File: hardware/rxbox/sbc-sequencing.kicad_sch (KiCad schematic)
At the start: 0 parts

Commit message: supervisor + symbol, new journal. jumper for t113 power
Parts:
- added C19, C20: 68nF, symbol Device:C_Small
- added C21: 640nF, symbol Device:C_Small
- added D1, D2, D3: 1N4148, symbol Device:D_Small_Filled
- added R13, R14, R15, R16, R19, R21: 1MR, symbol Device:R_Small_US
- added R17, R18, R20: 100kR, symbol Device:R_Small_US
- added R22: 47kR, symbol Device:R_Small_US
- added U8: ME2808A44, Package_TO_SOT_SMD:TSOT-23, symbol Power_Supervisor_Custom:ME2808X
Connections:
- net EN_CPU: now also C20.2, D2.2 (A), R18.1, R19.2
- net EN_SYS: now also C19.2, D1.2 (A), R16.2, R17.1
- new net 5V_PGOOD: D1.1 (K), D2.1 (K), D3.1 (K), R13.2, R14.2, R15.2, R17.2, R18.2, R20.2, R22.1, U8.1 (~{V_{OUT}})
- new net EN_CLK: C21.2, D3.2 (A), R20.1, R21.2
- new net Earth: C19.1, C20.1, C21.1, R13.1, R14.1, R15.1, R16.1, R19.1, R21.1, U8.2 (GND)
- new net T113_5V: R22.2, U8.3 (V_{IN})
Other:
- note added: "2.4ms"
- note added: "Power Supervisor"
- note added: "Wait for good 5V, first T sequence, 2.4ms later T1 sequence, 64ms T2 sequence"
- note added: "temporary: adjust for clock EN threshold"
- note removed: "0.9V"
- note removed: "0.9V/1.1V"
- note removed: "1.5V (DDR3)"
- note removed: "1.8V"
- note removed: "3.3V"
- note removed: "AVCC"
- note removed: "GENERAL"
- note removed: "Power Sequencing"
- note removed: "VCC_DRAM"
- note removed: "VDD_1V8"
- note removed: "VDD_CPU"
- note removed: "VDD_SYS"

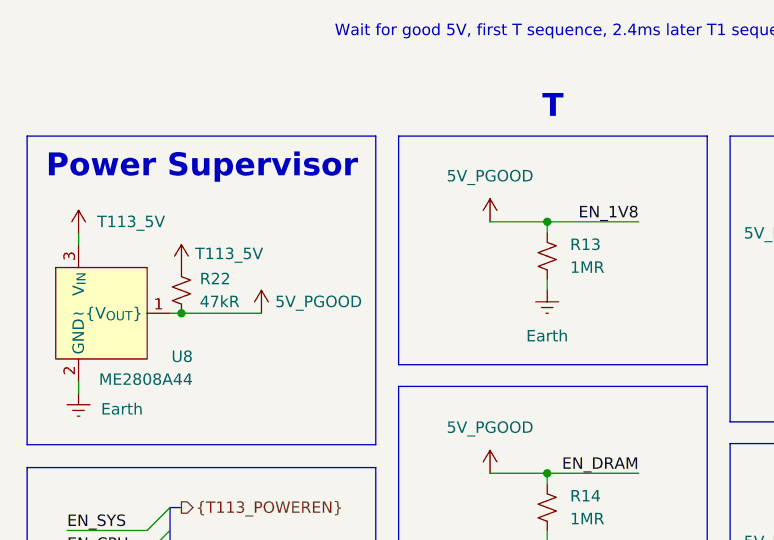
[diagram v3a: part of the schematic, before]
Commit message: finish hooking up wifi+bt, and power
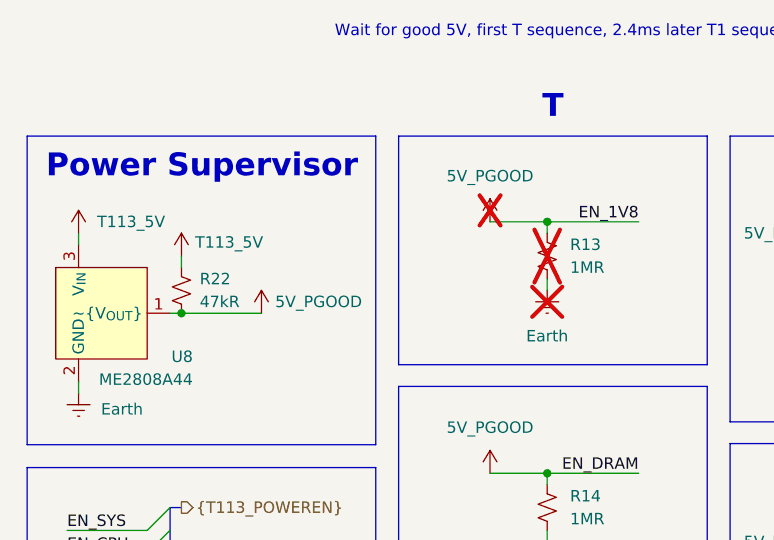
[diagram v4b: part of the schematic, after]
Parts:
- R13: now not fitted
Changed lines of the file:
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@@
 	(wire
 		(pts
+			(xy 48.26 71.12) (xy 48.26 72.39)
+		)
+		(stroke
+			(width 0)
+			(type default)
+		)
+	)
+	(wire
+		(pts
 			(xy 158.75 73.66) (xy 160.02 73.66)
 		)
@@
 	(symbol
 		(lib_id "power:+5V")
-		(at 48.26 72.39 0)
+		(at 48.26 71.12 0)
 		(unit 1)
 		(body_style 1)
@@
 		(dnp no)
 		(property "Reference" "#PWR040"
-			(at 48.26 76.2 0)
+			(at 48.26 74.93 0)
 			(hide yes)
 			(show_name no)
@@
 		)
 		(property "Value" "T113_5V"
-			(at 49.784 70.866 0)
+			(at 49.784 69.596 0)
 			(show_name no)
 			(do_not_autoplace no)
@@
 		)
 		(property "Footprint" ""
-			(at 48.26 72.39 0)
+			(at 48.26 71.12 0)
 			(hide yes)
 			(show_name no)
@@
 		)
 		(property "Datasheet" ""
-			(at 48.26 72.39 0)
+			(at 48.26 71.12 0)
 			(hide yes)
 			(show_name no)
@@
 		)
 		(property "Description" "Power symbol creates a global label with name \"+5V\""
-			(at 48.26 72.39 0)
+			(at 48.26 71.12 0)
 			(hide yes)
 			(show_name no)
@@
 		(on_board yes)
 		(in_pos_files yes)
-		(dnp no)
+		(dnp yes)
 		(fields_autoplaced yes)
 		(property "Reference" "#PWR023"
@@
 		(on_board yes)
 		(in_pos_files yes)
-		(dnp no)
+		(dnp yes)
 		(fields_autoplaced yes)
 		(property "Reference" "R13"
@@
 		(on_board yes)
 		(in_pos_files yes)
-		(dnp no)
+		(dnp yes)
 		(fields_autoplaced yes)
 		(property "Reference" "#PWR028"
